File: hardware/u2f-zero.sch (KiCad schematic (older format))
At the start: 12 parts, among them SW1 SW_PUSH

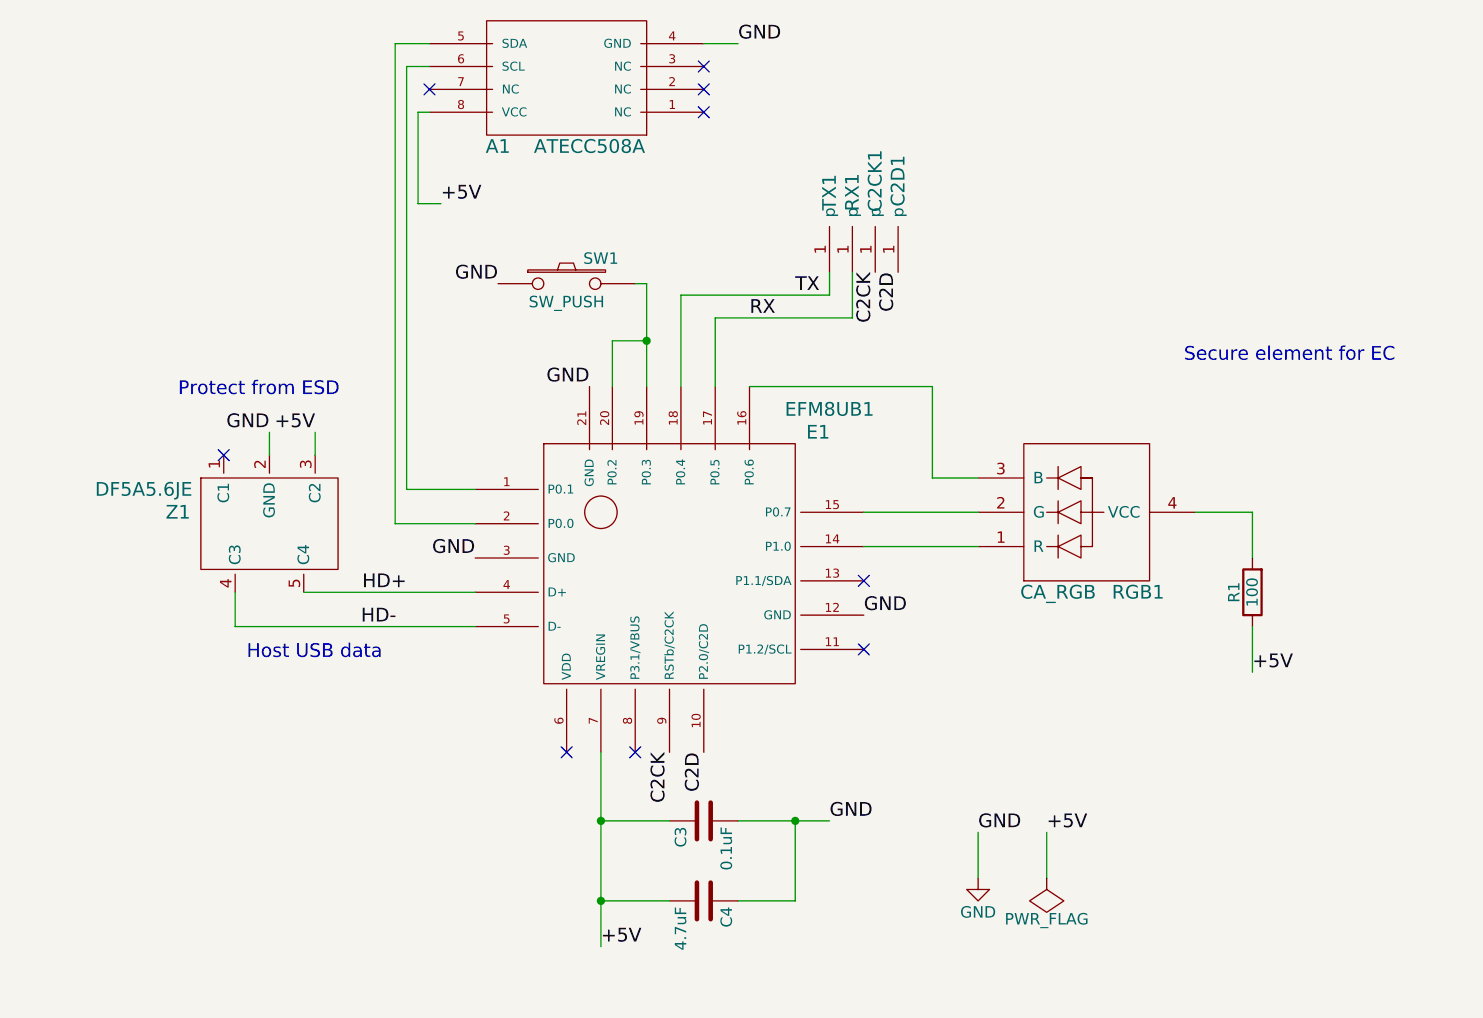
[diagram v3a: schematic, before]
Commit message: switched to qsop24 and soic8
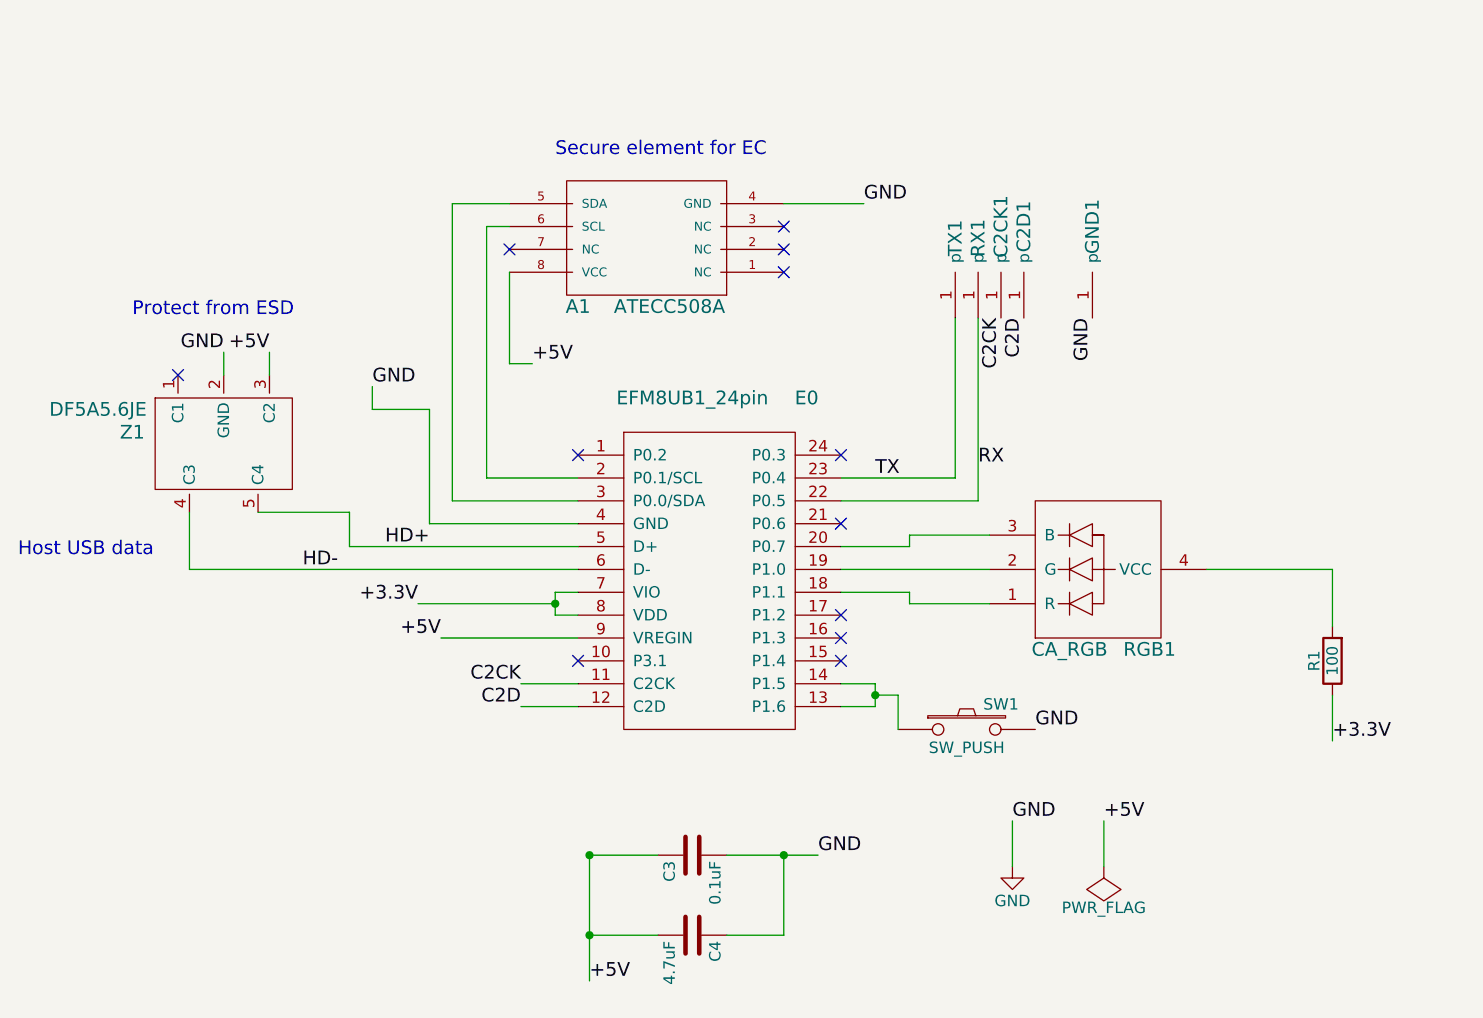
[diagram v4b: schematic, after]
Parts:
- removed E1: EFM8UB1, footprints:EFM8UB1, symbol EFM8UB1
- added E0: EFM8UB1_24pin, Housings_SSOP:SSOP-24_3.9x8.7mm_Pitch0.635mm, symbol EFM8UB1_24pin
- added GND1: debug-pin, footprints:debug, symbol debug-pin
- A1: footprint footprints:UDFN-8Pad -> Housings_SOIC:SOIC-8_3.9x4.9mm_Pitch1.27mm
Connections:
- net +5V: now also E0.9 (VREGIN); no longer R1.1
- net C2CK: now also E0.11 (C2CK)
- net C2D: now also E0.12 (C2D)
- net GND: now also SW1.2, E0.4 (GND), GND1.1 (p); no longer SW1.1
- net HD+: now also E0.5 (D+)
- net HD-: now also E0.6 (D-)
- net RX: now also E0.22 (P0.5)
- net TX: now also E0.23 (P0.4)
- net at A1.5 (SDA): now also E0.3 (P0.0/SDA)
- net at A1.6 (SCL): now also E0.2 (P0.1/SCL)
- net at RGB1.1 (R): now also E0.18 (P1.1)
- net at RGB1.2 (G): now also E0.19 (P1.0)
- net at RGB1.3 (B): now also E0.20 (P0.7)
- new net: E0.13 (P1.6), E0.14 (P1.5), SW1.1
- new net +3.3V: E0.7 (VIO), E0.8 (VDD), R1.1
- no-connect marks 9 -> 12
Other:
- moved on the sheet: A1, C2CK1, C2D1, C3, C4, R1, RGB1, RX1, SW1, TX1, Z1

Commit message: tweaks to qsop footprint and move resistor closer in
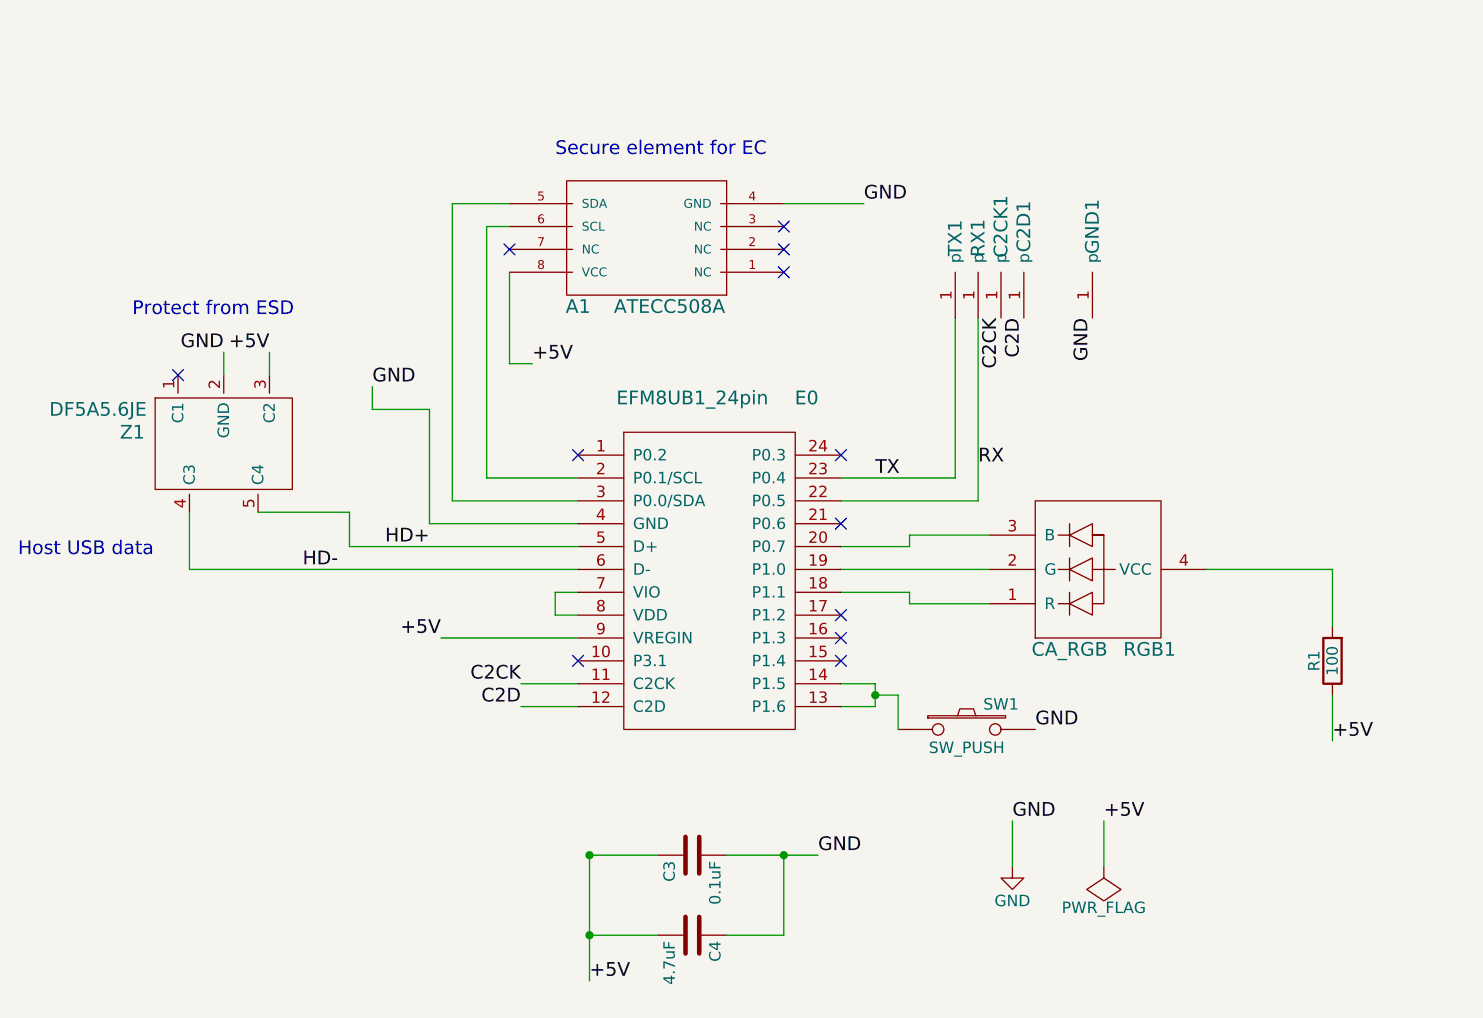
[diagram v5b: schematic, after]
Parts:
- E0: footprint Housings_SSOP:SSOP-24_3.9x8.7mm_Pitch0.635mm -> footprints:QSOP-24_3.9x8.7mm_Pitch0.635mm_fat
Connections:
- net +5V: now also R1.1
- net +3.3V: no longer names the net of E0.7 (VIO), E0.8 (VDD)
- net +3.3V: no longer R1.1
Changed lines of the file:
@@
 	8100 5050 8100 5250
 Text Label 8100 5250 0    60   ~ 0
-+3.3V
++5V
 Text Label 4550 5000 2    60   ~ 0
 C2CK
@@
 F 0 "E0" H 5800 4750 60  0000 C CNN
 F 1 "EFM8UB1_24pin" H 5300 4750 60  0000 C CNN
-F 2 "Housings_SSOP:SSOP-24_3.9x8.7mm_Pitch0.635mm" H 5650 4650 60  0001 C CNN
+F 2 "footprints:QSOP-24_3.9x8.7mm_Pitch0.635mm_fat" H 5650 4650 60  0001 C CNN
 F 3 "" H 5350 4250 60  0000 C CNN
 	1    5350 4250
@@
 	4800 4700 4700 4700
 Wire Wire Line
-	4700 4700 4700 4600
-Wire Wire Line
 	4700 4600 4800 4600
-Wire Wire Line
-	4700 4650 4100 4650
-Connection ~ 4700 4650
-Text Label 4100 4650 2    60   ~ 0
-+3.3V
 $Comp
 L debug-pin GND1
@@
 Text Label 7050 3400 3    60   ~ 0
 GND
+Wire Wire Line
+	4700 4700 4700 4600
 $EndSCHEMATC
